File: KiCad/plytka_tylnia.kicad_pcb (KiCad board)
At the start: 2 copper layers, 140 x 150 mm, 80 parts, among them J1 CONN_01X04, J2 CONN_01X04, J3 CONN_01X04, J4 CONN_01X04, J5 CONN_01X04, J6 CONN_01X04, J7 PIN10, J8 CONN_01X04, J9 CONN_01X04, P1 USB_OTG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

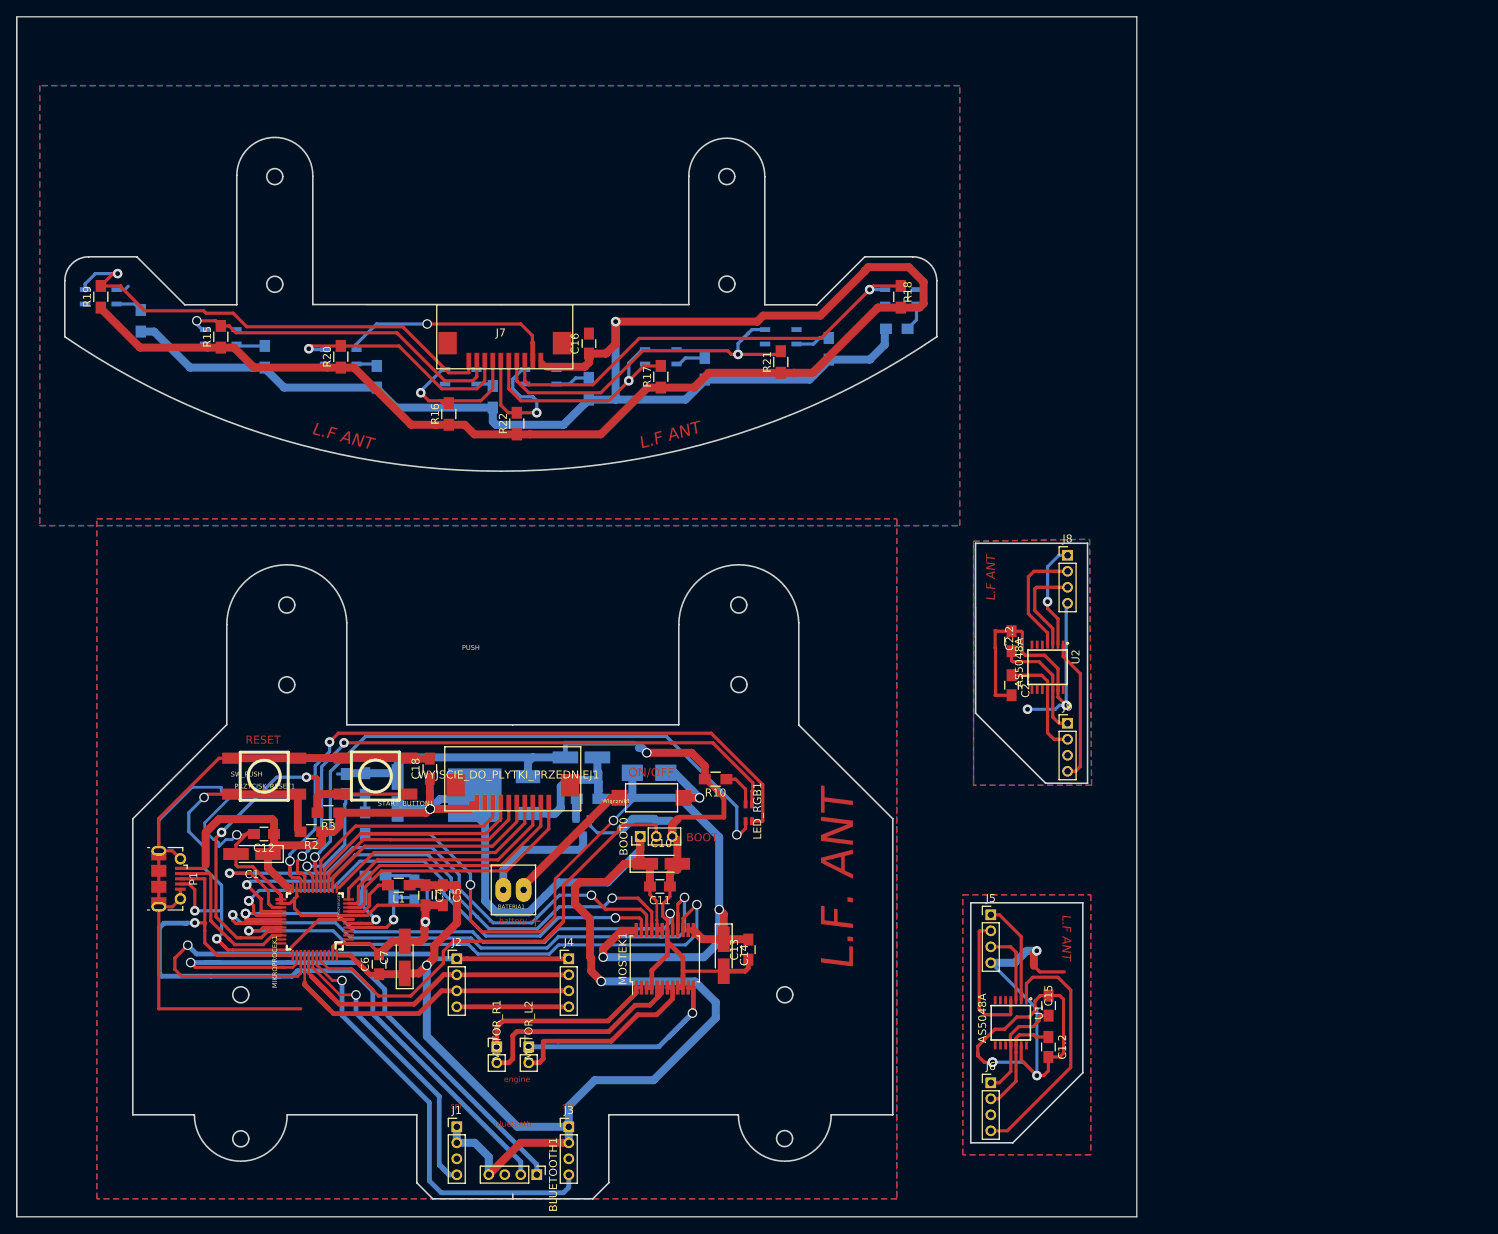
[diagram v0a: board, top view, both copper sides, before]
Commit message: zmienione przelotki na 1,4/0,5
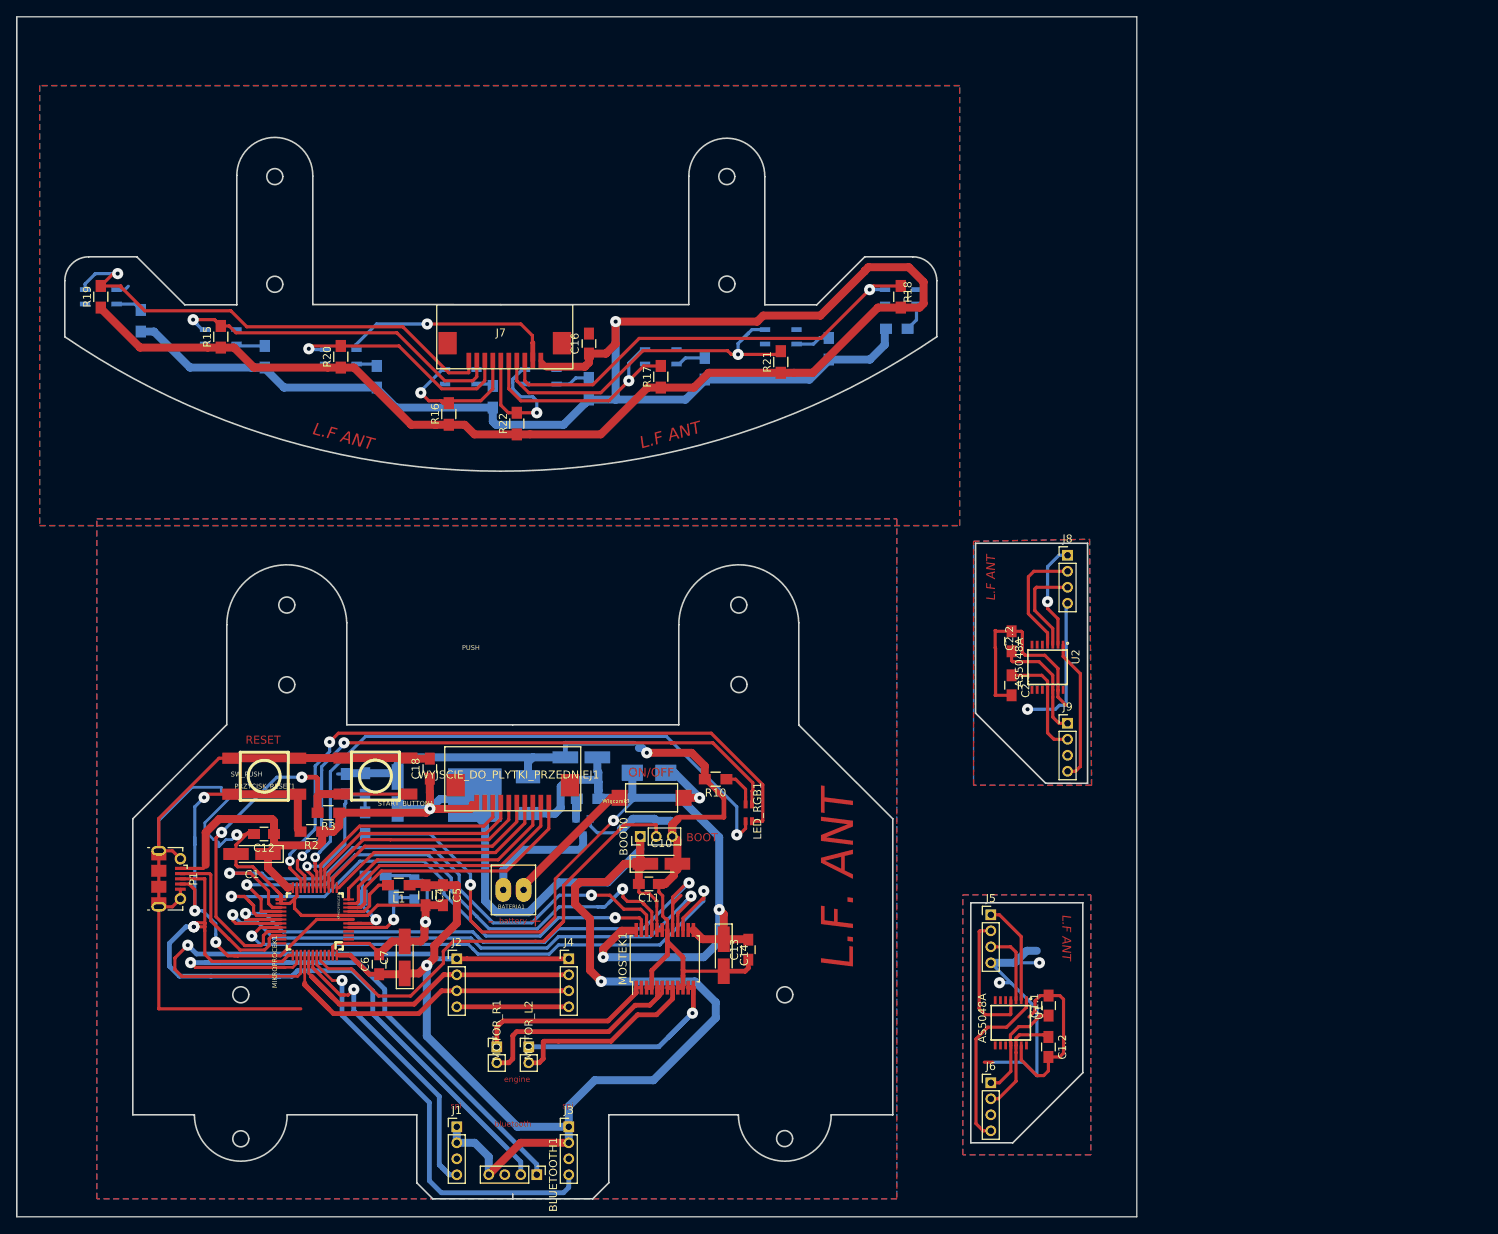
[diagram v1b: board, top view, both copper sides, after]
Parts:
- removed C15: C, Capacitors_SMD:C_0805_HandSoldering
- added C1.1: C, Capacitors_SMD:C_0805_HandSoldering, F.Cu at (164.0, 153.6)
- moved C11 1.42 mm to (114.0, 138.4)
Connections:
- net /L_IN1 renamed /L_1
- net /L_IN2 renamed /L_2
- net /R_IN1 renamed /R_1
- net /R_IN2 renamed /R_2
- J7 pad 10: /T1 -> /T1P
- J7 pad 3: /T8 -> /T8P
- J7 pad 4: /T7 -> /T7P
- J7 pad 5: /T6 -> /T6P
- J7 pad 6: /T5 -> /T5P
- J7 pad 7: /T4 -> /T4P
- J7 pad 8: /T3 -> /T3P
- J7 pad 9: /T2 -> /T2P
- R15 pad 2: /T2 -> /T2P
- R16 pad 2: /T4 -> /T4P
- R17 pad 2: /T6 -> /T6P
- R18 pad 2: /T8 -> /T8P
- R19 pad 2: /T1 -> /T1P
- R20 pad 2: /T3 -> /T3P
- R21 pad 2: /T7 -> /T7P
- R22 pad 2: /T5 -> /T5P
- T1 pad 4: /T2 -> /T2P
- T2 pad 4: /T4 -> /T4P
- T3 pad 4: /T6 -> /T6P
- T4 pad 4: /T8 -> /T8P
- T5 pad 4: /T1 -> /T1P
- T6 pad 4: /T3 -> /T3P
- T7 pad 4: /T5 -> /T5P
- T8 pad 4: /T7 -> /T7P
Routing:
- net /T1: track 93.6 -> 33.5 mm, vias 1 -> 0
- net /T1P: track 0.00 -> 60.1 mm, vias 0 -> 1
- net /T8: track 85.6 -> 28.6 mm, vias 1 -> 0
- net /T8P: track 0.00 -> 56.8 mm, vias 0 -> 1
- net /T7: track 74.4 -> 28.9 mm, vias 1 -> 0
- net /T7P: track 0.00 -> 45.5 mm, vias 0 -> 1
- net /T2P: track 0.00 -> 44.0 mm, vias 0 -> 1
- net /T2: track 74.1 -> 32.0 mm, vias 1 -> 0
- net /T6P: track 0.00 -> 29.9 mm, vias 0 -> 1
- net /T6: track 59.0 -> 29.1 mm, vias 1 -> 0
- net /T3P: track 0.00 -> 29.4 mm, vias 0 -> 1
- net /T3: track 59.8 -> 30.5 mm, vias 1 -> 0
- net /T4P: track 0.00 -> 19.0 mm, vias 0 -> 1
- net /T4: track 48.4 -> 29.4 mm, vias 1 -> 0
- net /T5: track 48.3 -> 29.5 mm, vias 1 -> 0
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
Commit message: raster goldpin na 2,54, scieżki wokół procka i mostka na 0,3 mm,
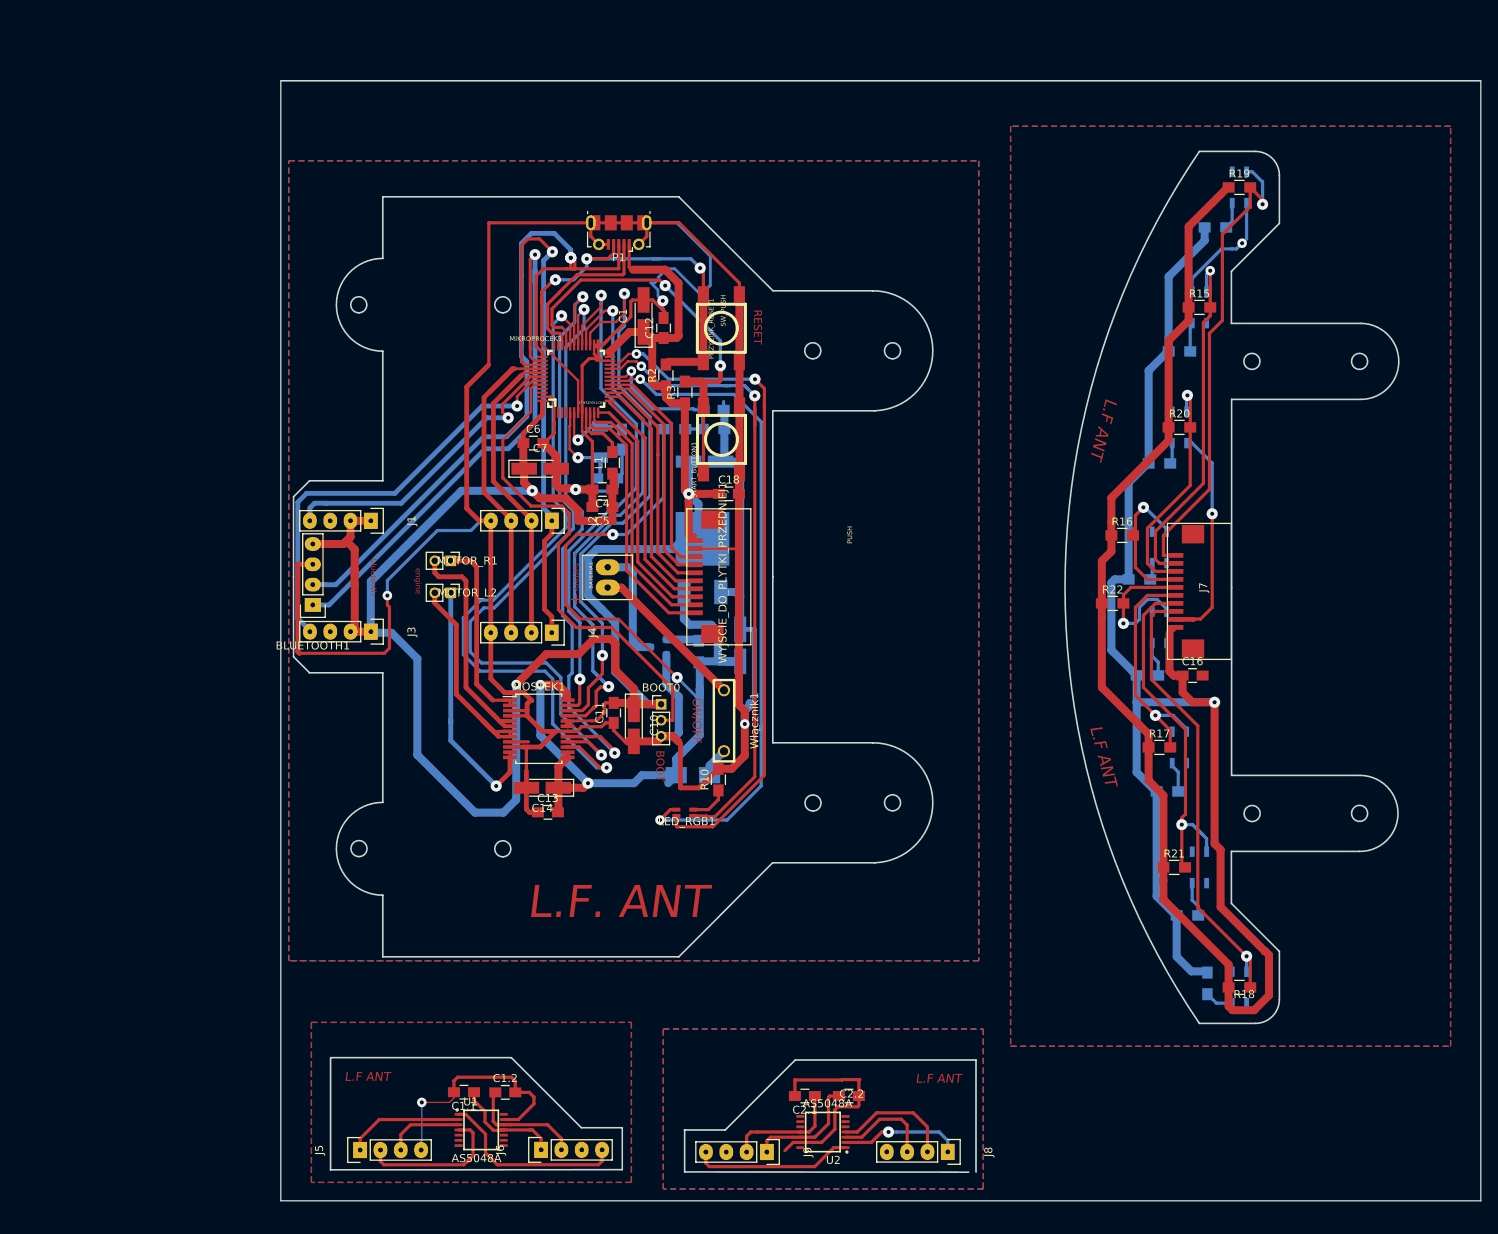
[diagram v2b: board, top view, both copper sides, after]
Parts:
- BLUETOOTH1, J1, J2, J3, J4, J5, J6, J8, J9: footprint Pin_Headers:Pin_Header_Straight_1x04_Pitch2.00mm -> 111:GoldPin_1x4
- TRANSISTOR1: footprint misc:SOT23-3 -> TO_SOT_Packages_SMD:SOT-23
- Włącznik1: footprint misc:tact_switch_smd -> misc:dip_switch_1
- moved R19 143.0 mm to (187.8, 51.3), turned to 0 degrees
- moved T5 143.0 mm to (187.8, 51.3), turned to 0 degrees
- moved R11 134.8 mm to (184.8, 56.3), turned to 0 degrees
- moved R15 122.4 mm to (182.8, 66.3), turned to 0 degrees
- moved T1 122.4 mm to (182.8, 66.3), turned to 0 degrees
- moved R1 114.3 mm to (180.3, 71.8), turned to 0 degrees
- moved R20 105.2 mm to (180.3, 81.3), turned to 0 degrees
- moved T6 105.2 mm to (180.3, 81.3), turned to 0 degrees
- moved P1 99.7 mm to (110.2, 56.1), turned to 180 degrees
- moved R12 98.4 mm to (177.8, 85.8), turned to 0 degrees
- moved R18 96.1 mm to (187.8, 151.3), turned to 0 degrees
- moved T4 96.1 mm to (187.8, 151.3), turned to 0 degrees
- moved J7 92.2 mm to (182.8, 102.3), turned to 90 degrees
- moved R9 90.6 mm to (183.8, 150.8), turned to 270 degrees
- moved T2 89.9 mm to (177.8, 96.3), turned to 0 degrees
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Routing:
- net GND: track 358.3 -> 499.5 mm, vias 4 -> 6
- net /GND1: track 61.1 -> 29.8 mm, vias 2 -> 1
- net /GND2: track 44.4 -> 26.8 mm, vias 1 -> 0
- net /R_PWM: track 72.3 -> 87.4 mm
- net /R_1: track 74.5 -> 89.2 mm
- net VCC: track 572.0 -> 582.5 mm
- net /LED_B: track 78.2 -> 84.4 mm
- net /SPI1_SS1: track 46.0 -> 40.7 mm
- net /LED_R: track 77.4 -> 81.7 mm
- net Net-(Bezpiecznik1-Pad2): track 7.53 -> 3.75 mm, vias 1 -> 0
- net Net-(BATERIA1-Pad2): track 17.1 -> 20.4 mm
- net /BATERIA: track 144.4 -> 141.2 mm
- net /L_PWM: track 68.8 -> 66.1 mm
- net Net-(MOSTEK1-Pad7): track 25.0 -> 27.2 mm
- net /SS2: track 18.0 -> 20.0 mm
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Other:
- board size 140 x 150 mm -> 150 x 140 mm
- board text removed: "spi"
